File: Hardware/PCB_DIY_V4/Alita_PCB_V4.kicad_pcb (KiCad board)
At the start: 2 copper layers, 100 x 55 mm, 30 parts, among them J1 Interface, J2 Vss, J4 Conn_01x03_Pin, J5 Driver, J6 MUX_header1, J7 MUX_header2, P1 5v_Pins, P2 3.3v_Pins, U1 MUX 4067, U2 ESP32_NODEMCU

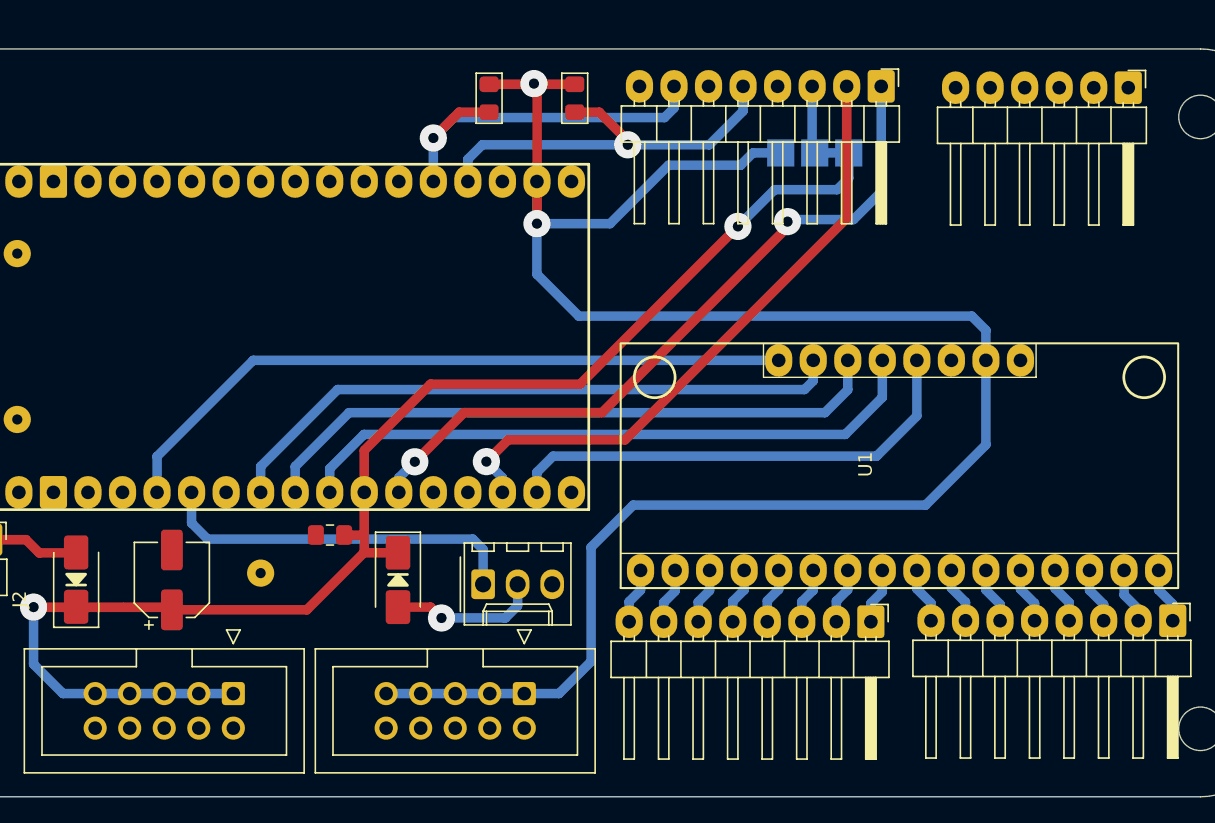
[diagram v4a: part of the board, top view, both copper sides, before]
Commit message: Ruteo y PCB completada
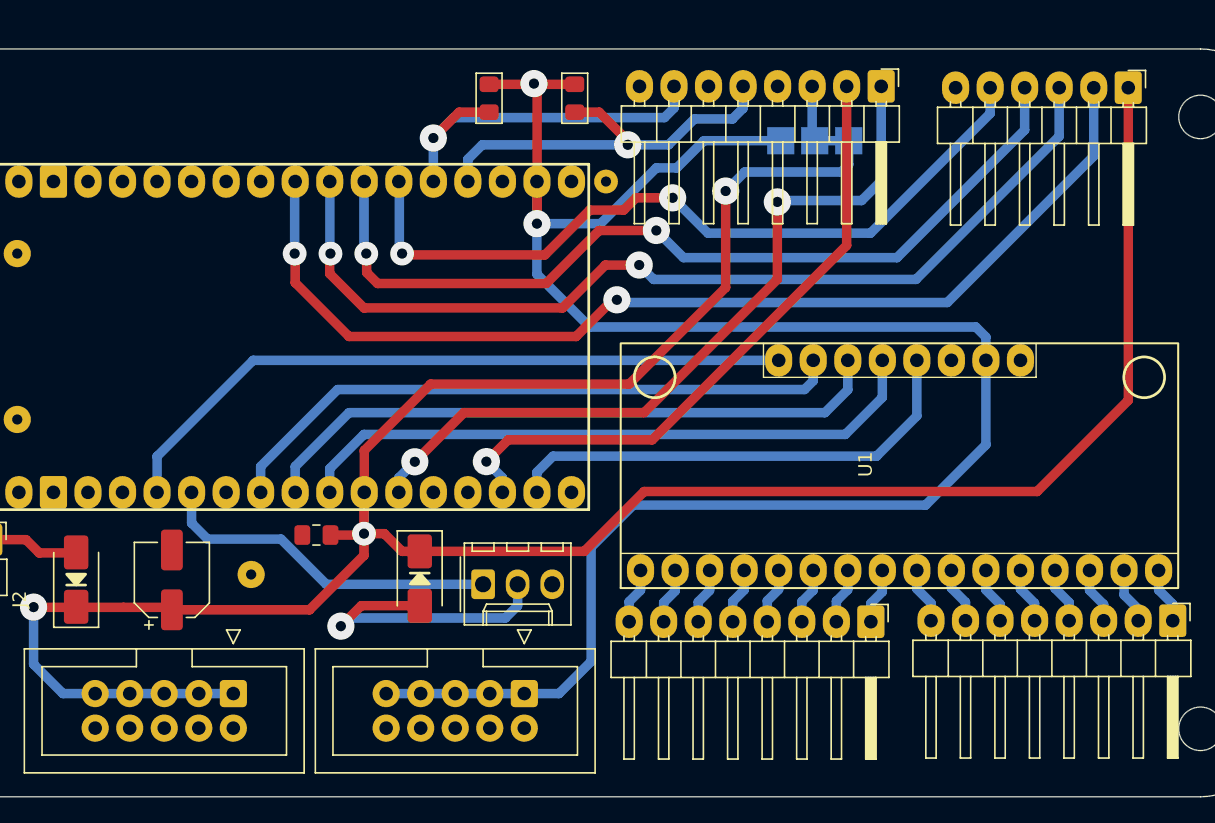
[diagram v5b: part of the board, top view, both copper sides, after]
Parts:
- added ?: , , F.Cu at (151.8, 100.1)
- moved D2 1.60 mm to (138.1, 129.3)
- moved C2 1.00 mm to (130.5, 126.1)
- moved JP1 0.90 mm to (167.0, 97.2)
- moved ? 0.71 mm to (125.7, 129.0)
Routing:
- net +5V: track 103.6 -> 194.2 mm, vias 2 -> 3
- net /MB2: track 0.00 -> 78.5 mm, vias 0 -> 2
- net /MB1: track 0.00 -> 71.2 mm, vias 0 -> 2
- net /MA2: track 0.00 -> 65.0 mm, vias 0 -> 2
- net /MA1: track 0.00 -> 57.1 mm, vias 0 -> 2
- net Net-(D2-A): track 11.1 -> 21.6 mm
- net /SDA: track 53.3 -> 55.9 mm
- net /ESC: track 27.1 -> 25.6 mm
- net /SCL: track 46.4 -> 47.5 mm
- net Net-(J1-Pin_3): track 4.98 -> 4.08 mm

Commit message: Primera revisión PCB
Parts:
- removed the ? at (151.8, 100.1)
- moved ? 1.70 mm to (197.6, 103.8)
- moved ? 1.70 mm to (197.6, 113.8)
- moved ? 1.70 mm to (197.6, 118.8)
- moved ? 1.70 mm to (197.6, 123.8)
- moved ? 1.70 mm to (197.6, 108.8)
- moved ? 1.70 mm to (197.6, 128.8)
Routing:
- net /MA2: track 65.0 -> 63.9 mm
- net /MA1: track 57.1 -> 56.1 mm
- net /MB1: track 71.2 -> 70.5 mm

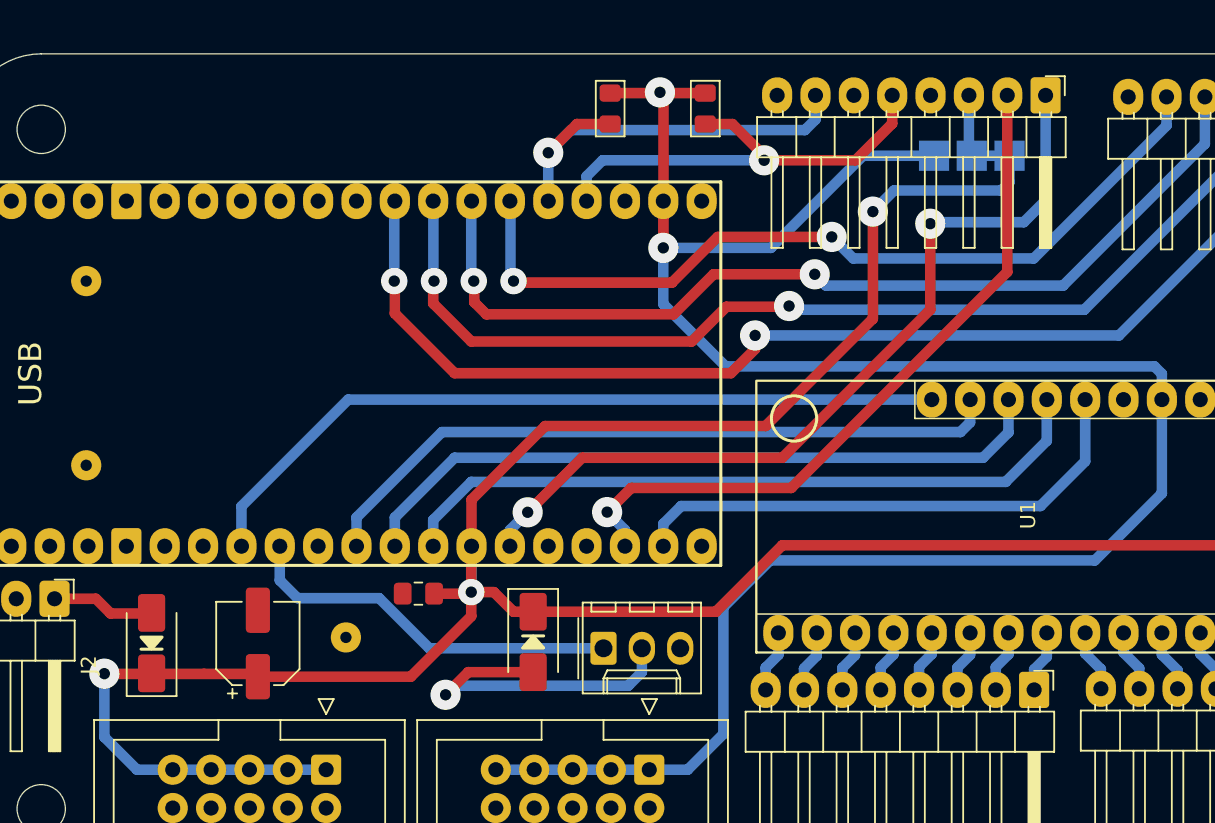
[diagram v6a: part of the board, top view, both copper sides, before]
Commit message: PCB_V4: Pinout del ESP32 arreglado
el driver estaba conectado a los pines de input only jeje
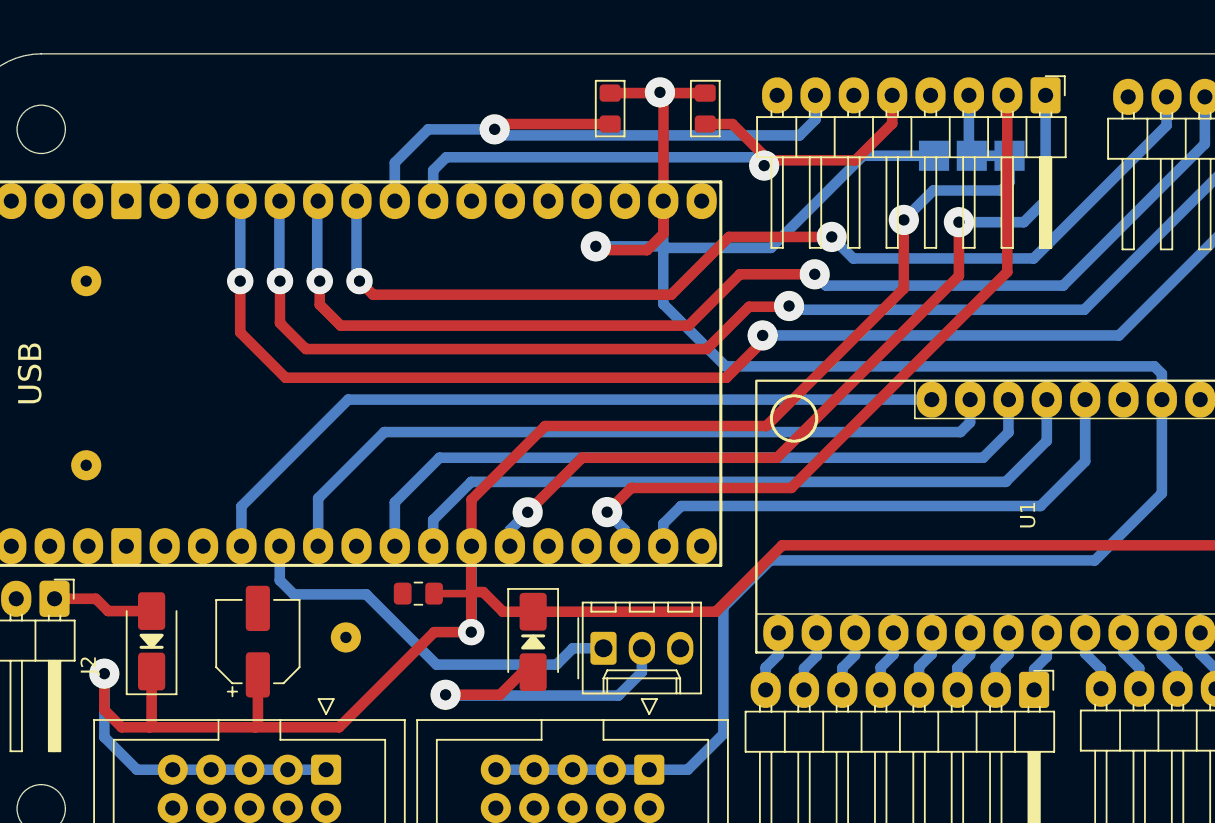
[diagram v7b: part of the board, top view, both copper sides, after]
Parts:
- moved C1 0.12 mm to (119.9, 129.3)
- moved D1 0.12 mm to (112.8, 129.3)
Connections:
- U2 pad 10: unconnected-(U2-GPIO25-Pad10) -> /MA1
- U2 pad 11: unconnected-(U2-GPIO26-Pad11) -> /MA2
- U2 pad 12: unconnected-(U2-GPIO27-Pad12) -> /MB1
- U2 pad 13: /P14 -> /MB2
- U2 pad 14: /P12 -> unconnected-(U2-GPIO12-Pad14)
- U2 pad 23: /P15 -> unconnected-(U2-GPIO15-Pad23)
- U2 pad 28: unconnected-(U2-GPIO17-Pad28) -> /S3
- U2 pad 29: /S3 -> unconnected-(U2-GPIO5-Pad29)
- U2 pad 4: /Button1 -> unconnected-(U2-GPIO36-Pad4)
- U2 pad 5: /Button2 -> unconnected-(U2-GPIO39-Pad5)
- U2 pad 6: /MA1 -> unconnected-(U2-GPIO34-Pad6)
- U2 pad 7: /MA2 -> unconnected-(U2-GPIO35-Pad7)
- U2 pad 8: /MB1 -> /Button1
- U2 pad 9: /MB2 -> /Button2
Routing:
- net +5V: track 194.2 -> 207.7 mm
- net /Button2: track 28.3 -> 41.4 mm
- net /MB1: track 70.5 -> 81.9 mm
- net /Button1: track 30.3 -> 41.5 mm
- net /MB2: track 78.9 -> 89.9 mm
- net /MA2: track 63.9 -> 74.7 mm
- net /MA1: track 56.1 -> 66.6 mm
- net +3.3V: track 142.3 -> 150.9 mm
- net /S3: track 46.7 -> 49.9 mm
- net /SDA: track 55.9 -> 54.6 mm
- net /ESC: track 25.6 -> 26.5 mm
- net /S2: track 47.0 -> 47.6 mm

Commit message: PCB_V4: conexion a GND de C1 arreglada
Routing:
- net GND: track 0.00 -> 2.94 mm
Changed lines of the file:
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@@
+	)
+	(segment
+		(start 119.87 127.0775)
+		(end 116.9275 127.0775)
+		(width 0.5)
+		(layer "F.Cu")
+		(net 1)
 	)
 	(segment
